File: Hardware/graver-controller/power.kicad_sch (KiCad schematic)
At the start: 36 parts, among them J101 DC jack 5.5x2.1, Q101 DMP6023LE, U101 LM5164DDAR, U102 AP2112K-3.3

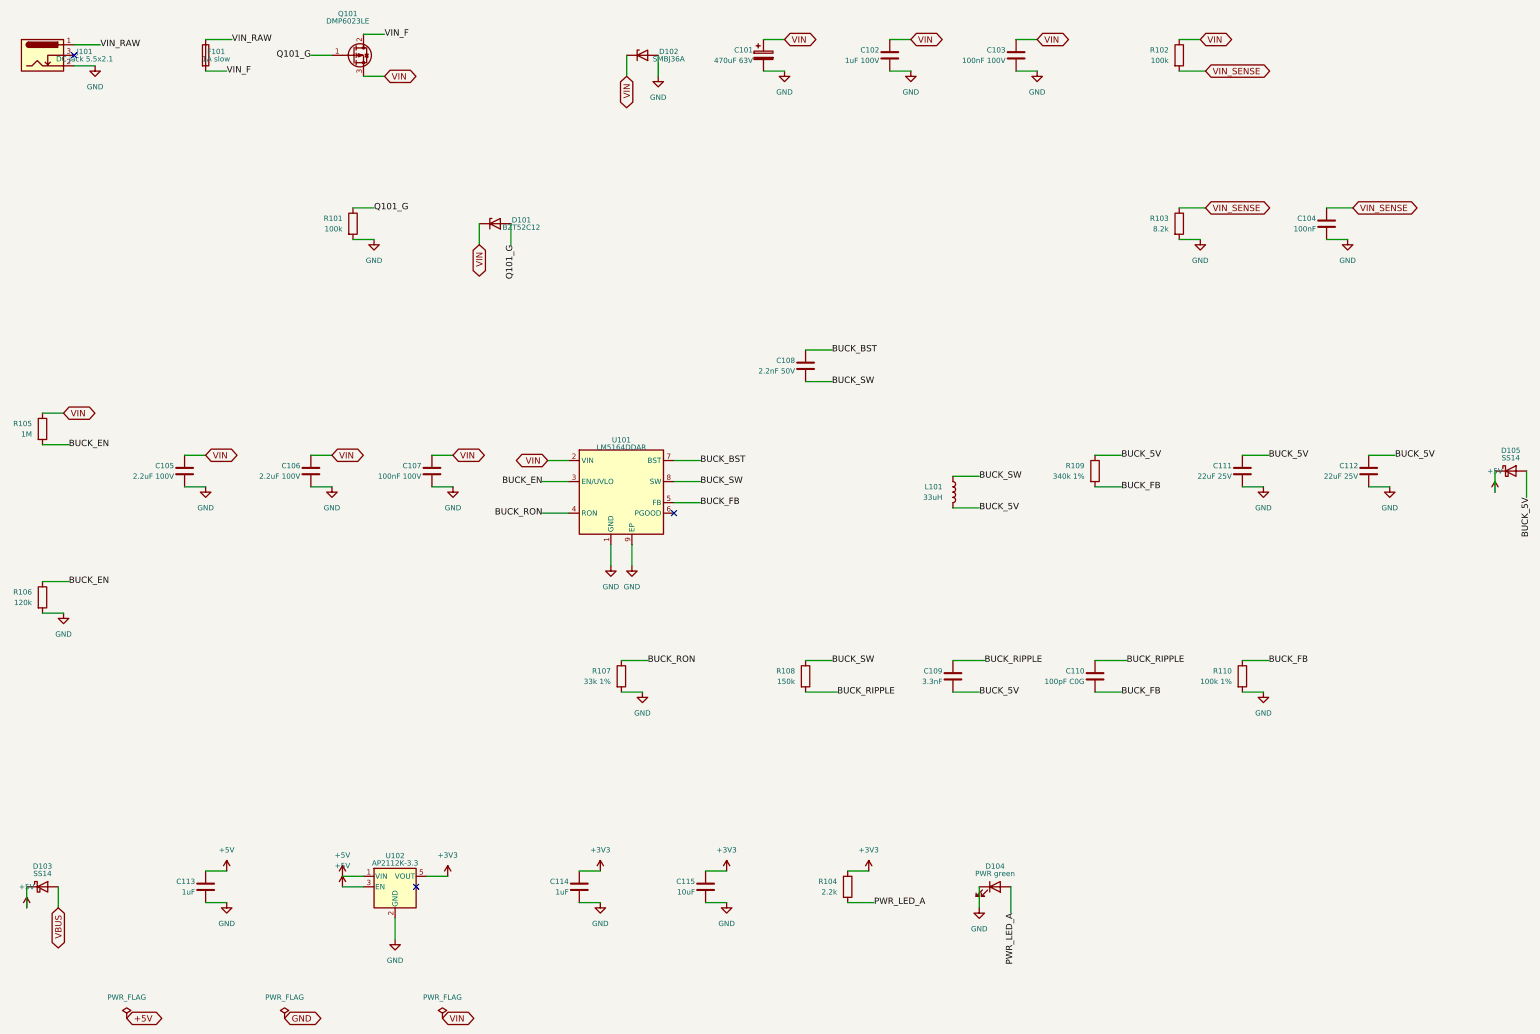
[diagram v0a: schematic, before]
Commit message: hardware: redraw the four schematic sheets with real wiring
The captured sheets connected everything by name with parts scattered on
the page. The sheets are now generated from hand-designed layouts
(Hardware/graver-controller/tools): decoupling caps drawn at their pins,
signal flow left to right, wires inside each block, global labels only
where a net crosses sheets. Power is two rows, MCU and IO fit A4.

Circuit unchanged: verify.sh compares the XML netlist against the
captured sheets kept in tools/ref (117 components with values,
footprints and LCSC fields, 65 nets by pin set) - identical. ERC: 0
violations. Q203 uses the generic Q_NMOS_GSD symbol (value BSS123),
which removes the library-mismatch warning.
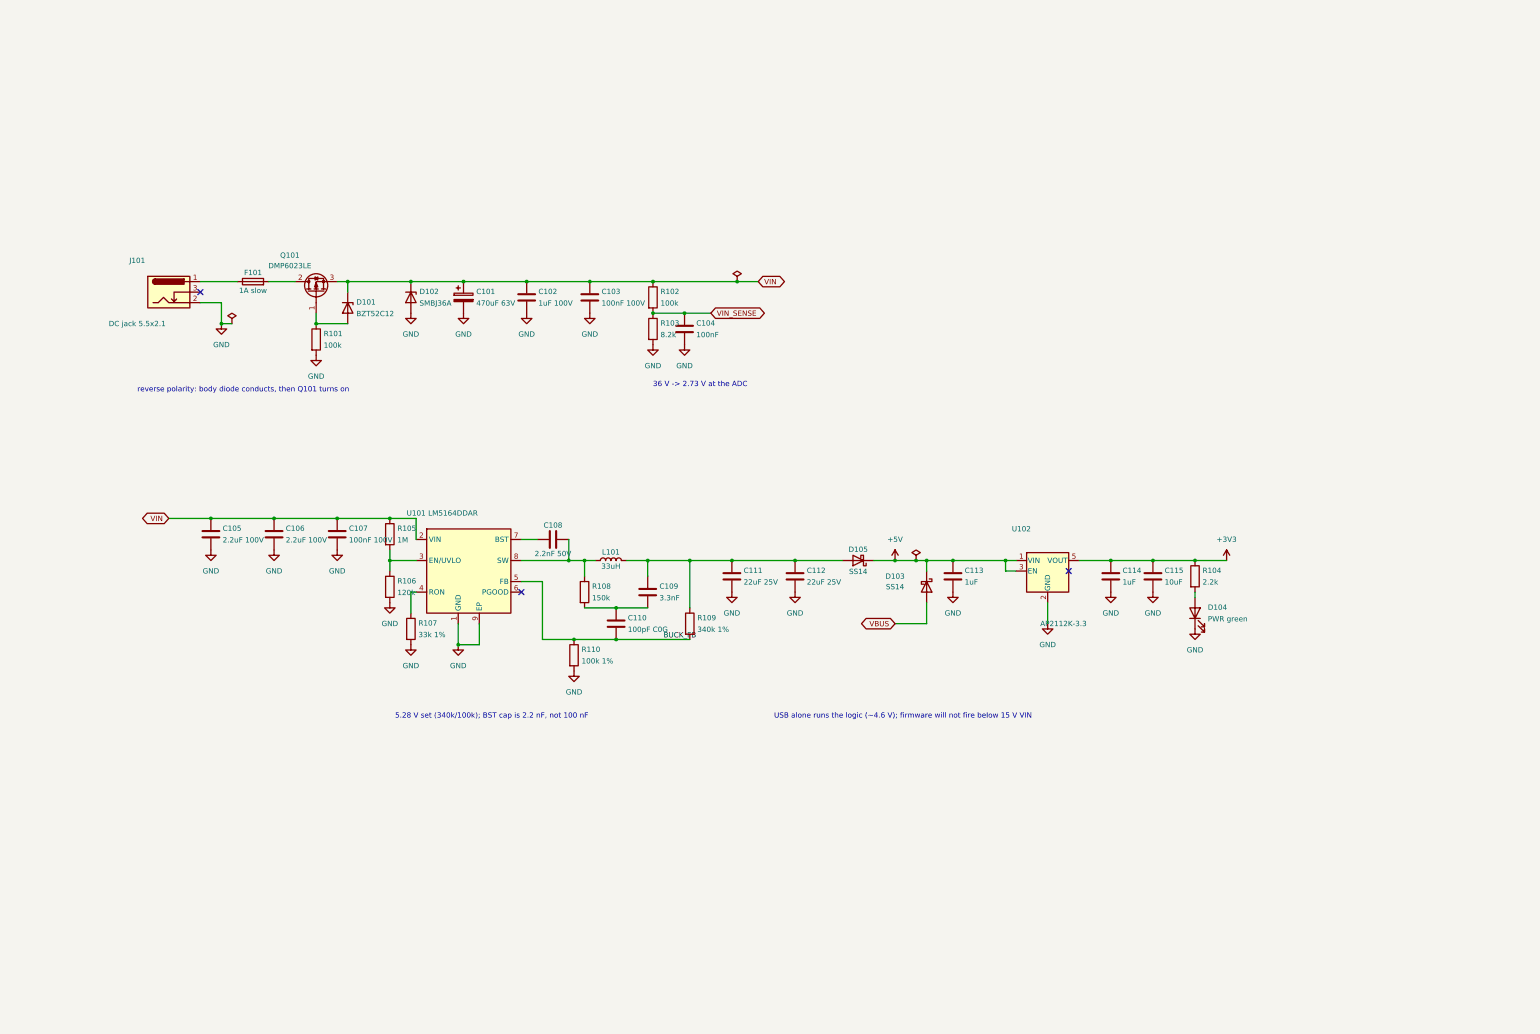
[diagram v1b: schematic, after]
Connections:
- net BUCK_5V: no longer names the net of C109.2, C111.1, C112.1, D105.2 (A), L101.2, R109.1
- net BUCK_BST: no longer names the net of C108.1, U101.7 (BST)
- net BUCK_EN: no longer names the net of R105.2, R106.1, U101.3 (EN/UVLO)
- net BUCK_RIPPLE: no longer names the net of C109.1, C110.1, R108.2
- net BUCK_RON: no longer names the net of R107.1, U101.4 (RON)
- net BUCK_SW: no longer names the net of C108.2, L101.1, R108.1, U101.8 (SW)
- net PWR_LED_A: no longer names the net of D104.2 (A), R104.2
- net Q101_G: no longer names the net of D101.2 (A), Q101.1 (G), R101.1
- net VIN_F: no longer names the net of F101.2, Q101.2 (D)
- net VIN_RAW: no longer names the net of F101.1, J101.1
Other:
- note added: "36 V -> 2.73 V at the ADC"
- note added: "5.28 V set (340k/100k); BST cap is 2.2 nF, not 100 nF"
- note added: "USB alone runs the logic (~4.6 V); firmware will not fire below 15 V VIN"
- note added: "reverse polarity: body diode conducts, then Q101 turns on"
